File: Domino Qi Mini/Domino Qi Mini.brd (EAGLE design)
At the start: 55.9 x 33 mm, 94 parts, among them J1 MH22-1, J2 MH22-1, M1 DOMINO, Q1 AP2302GN, Q2 2SC4081, SW1 IT-1210, SW2 IT-1210, SW3 IT-1210, U1 MP65151DJ, U2 ATMEGA32U4-AU/MU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

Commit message: Domino Qi Mini Rev. C: changed NTB0102GU to NTB0102GF
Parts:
- U5: value NTB0102GU -> NTB0102GF; device Domino:XQFN-10 -> Domino:SOT1089
- moved C21 3.30 mm to (15.6, 22.9), turned to 0 degrees
- moved C27 3.30 mm to (16.0, 25.5), turned to 0 degrees
- moved R19 2.99 mm to (17.8, 22.7), turned to 0 degrees
- moved R10 1.05 mm to (14.6, 24.4), turned to 270 degrees
- moved U5 0.13 mm to (16.8, 24.1), turned to 180 degrees
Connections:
- net +2V5: now also U5.3; no longer U5.2
- net +5V: now also U5.7; no longer U5.6
- net GND: now also U5.2; no longer U5.9
- net GP6: now also U5.1; no longer U5.5
- net I2S_MICIN: now also U5.6; no longer U5.4
- net I2S_WS: now also U5.5; no longer U5.10
- net JTAG_TDI: now also U5.4; no longer U5.1
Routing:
- net HANDSHAKE: track 35.1 -> 38.3 mm, vias 2 -> 3
- net GND: track 5.96 -> 8.85 mm, vias 234 -> 235
- net +2V5: track 37.8 -> 40.4 mm
- net LED8: track 19.5 -> 21.5 mm
- net LED6: track 65.0 -> 66.6 mm
- net I2S_WS: track 50.9 -> 51.5 mm
- net I2S_MICIN: track 52.8 -> 52.2 mm

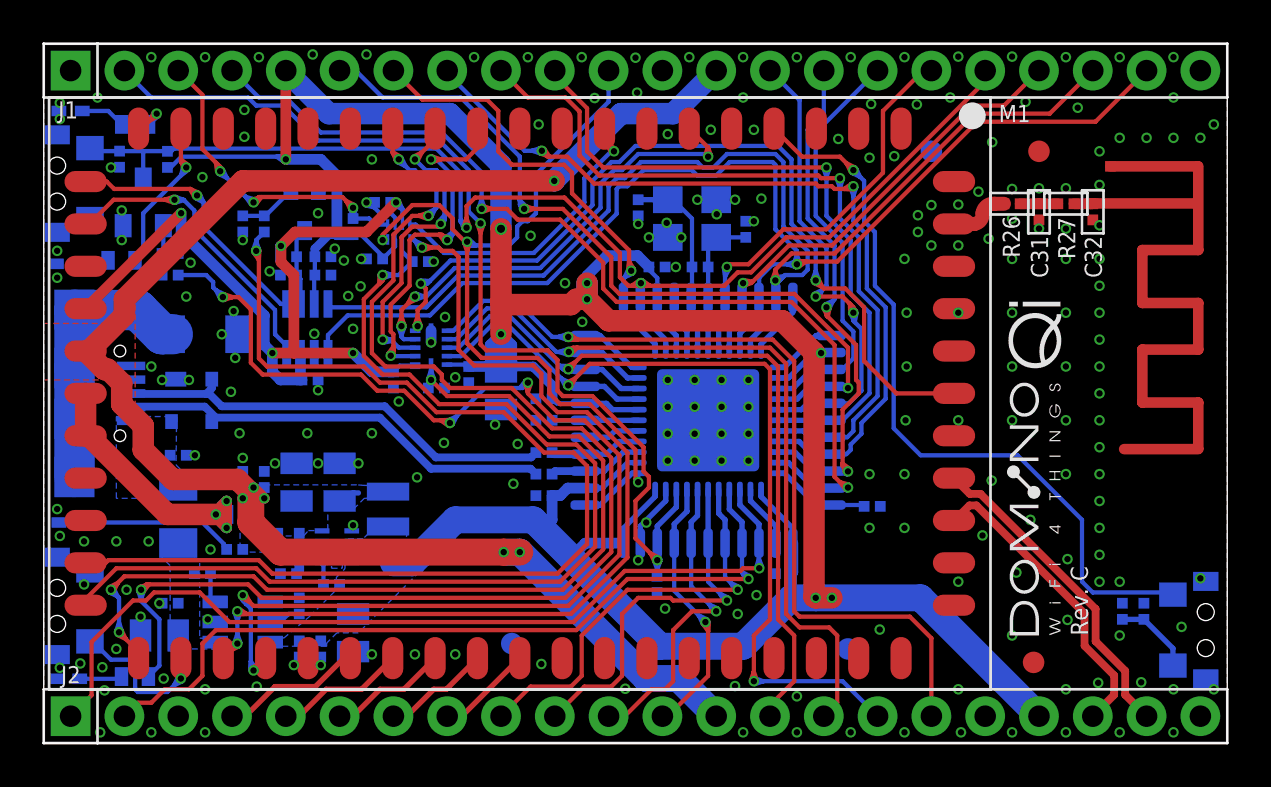
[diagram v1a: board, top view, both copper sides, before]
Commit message: Domino Qi Mini Rev. D: corrected bridge pinout
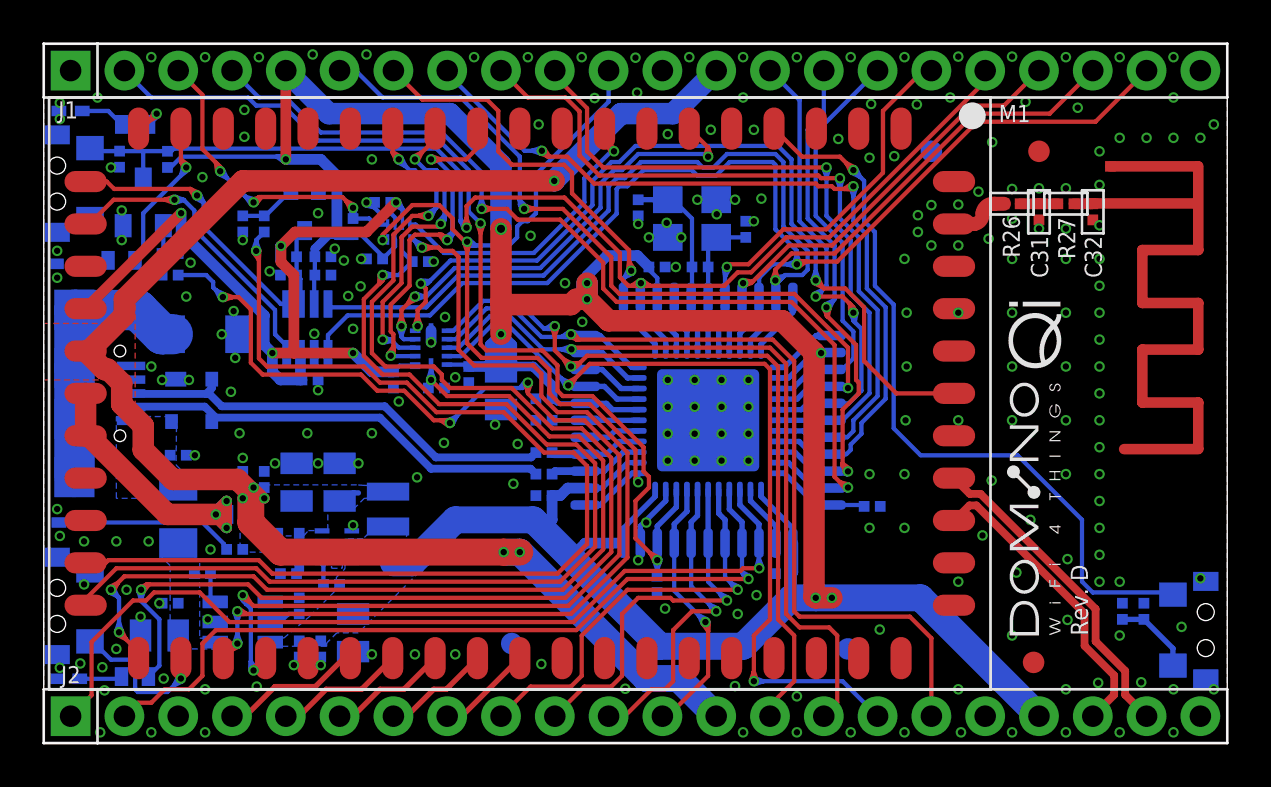
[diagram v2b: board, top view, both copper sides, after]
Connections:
- net MISO: now also U4.8; no longer U4.7
- net MOSI: now also U4.9; no longer U4.8
- net SCK: now also U4.7; no longer U4.9
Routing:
- net SCK: track 39.3 -> 42.5 mm, vias 1 -> 2
- net MOSI: track 40.9 -> 39.4 mm

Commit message: Changed Domino Qi Mini to 4 layers
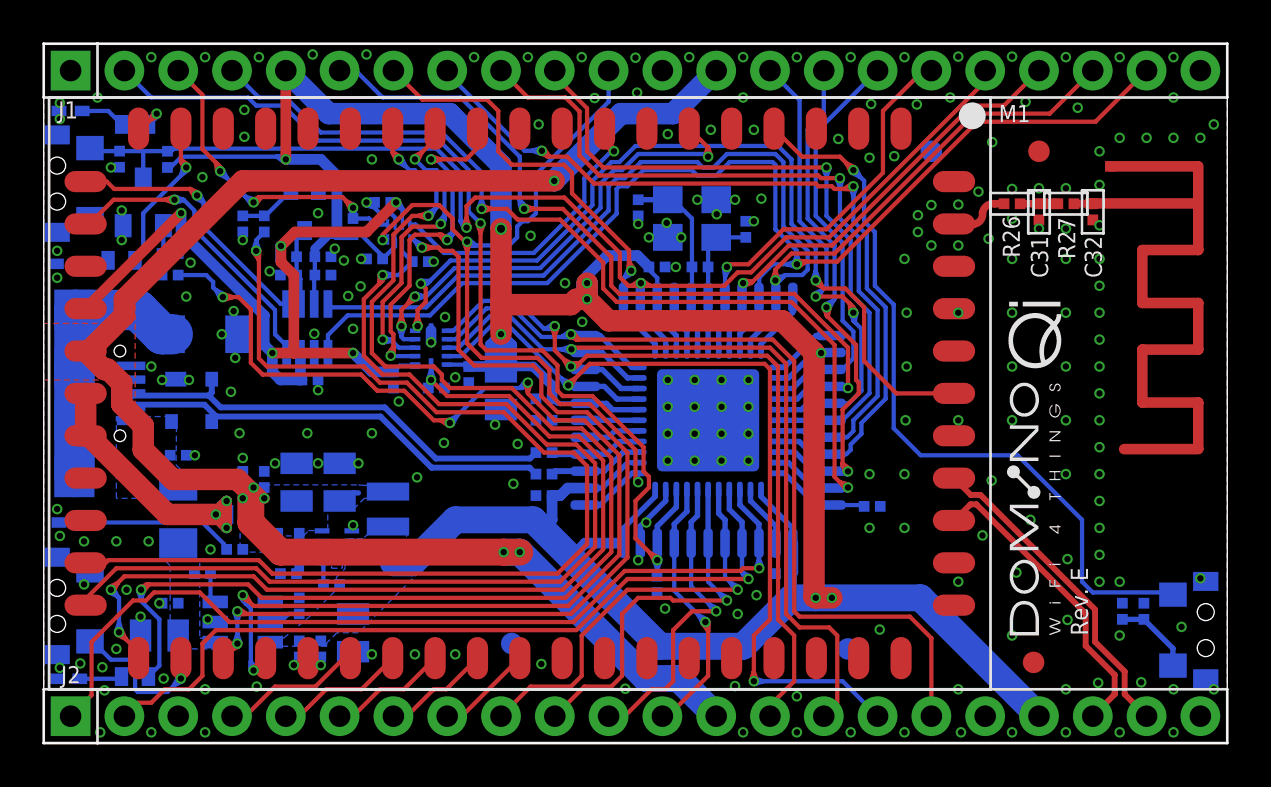
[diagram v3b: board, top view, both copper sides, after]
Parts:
- moved DRILEGEND 1.27 mm to (96.8, 62.5)
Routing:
- added copper zone on layer 15, net GND
- added copper zone on layer 2, net GND
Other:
- board text added: "* 4 COPPER LAYERS"
- board text added: "0.132 MM PREPREG FR-4"
- board text added: "0.6 MM CORE FR-4 LG 135 INC. COP."
- board text added: "1.00 MM+/-10%"
- board text added: "11 mils"
- board text added: "14 mils"
- board text added: "18 UM CU + 18 UM PLATING (35 UM)"
- board text added: "35 UM COPPER"
- board text added: "8 mils"
- board text added: "LAYER 2 L2 GND"
- board text added: "LAYER 3 L15 GND"
- board text added: "PREPREG"
- board text removed: "* 2 COPPER LAYERS"
- board text removed: "1.0 MM CORE FR-4 LG 135 INCLUDING COPPER"
- board text removed: "1.061 MM+/-10%"
- board text removed: "10 mils"
- board text removed: "14.5 mils"
- board text removed: "18 UM CU + 12.5 UM PLATING (30.5 UM)"
- board text removed: "26 mils"
